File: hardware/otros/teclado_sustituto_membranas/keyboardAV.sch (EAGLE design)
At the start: 99 parts, among them IC1 74HC32, IC2 74LS244DW

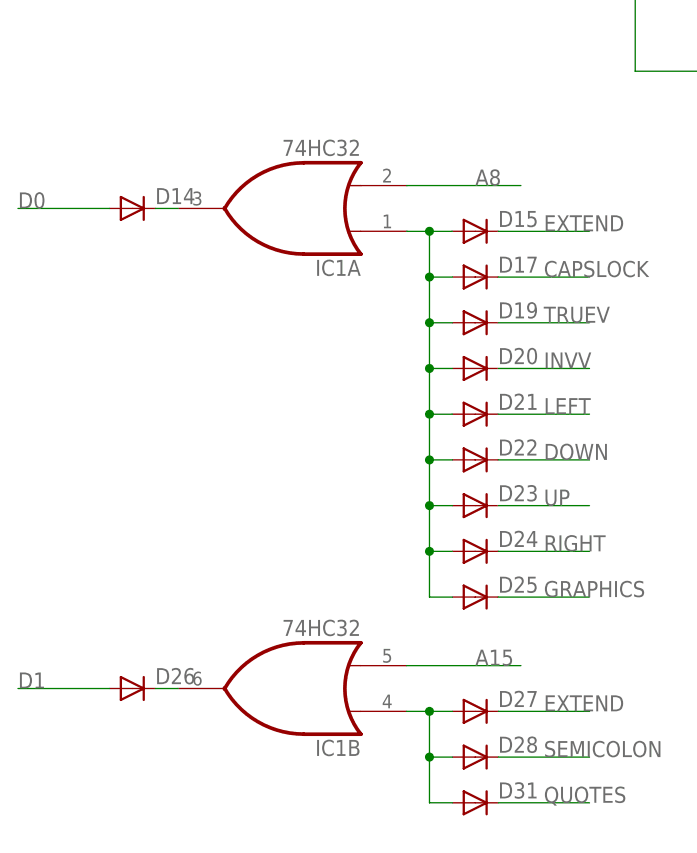
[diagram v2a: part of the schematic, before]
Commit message: 
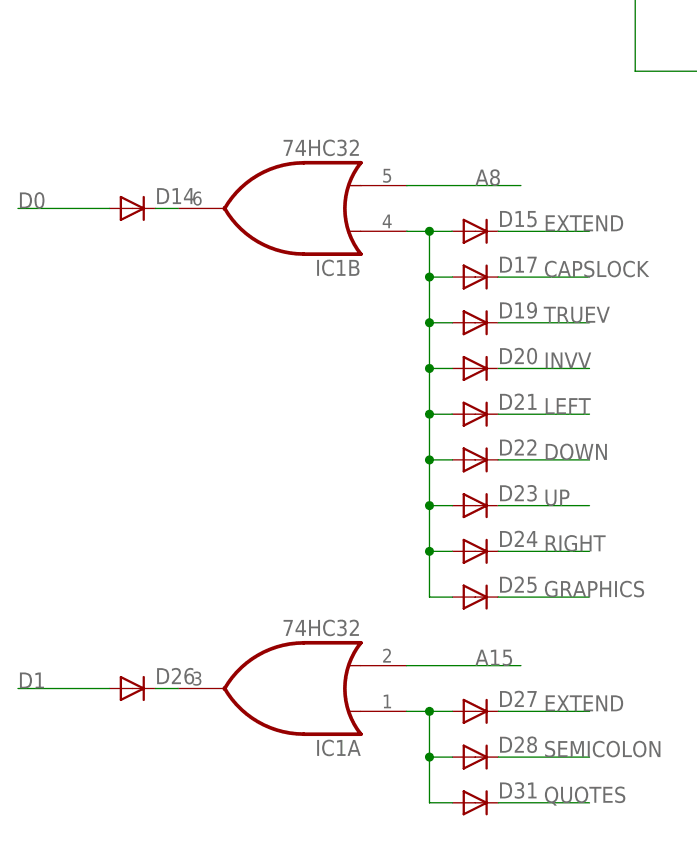
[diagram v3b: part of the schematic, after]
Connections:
- net A15: now also IC1A.I1; no longer IC1B.I1
- net A8: now also IC1B.I1; no longer IC1A.I1
- net N$84: now also IC1B.O; no longer IC1A.O
- net N$86: now also IC1A.O; no longer IC1B.O
- net N$87: now also IC1A.I0; no longer IC1B.I0
- net N$90: now also IC1B.I0; no longer IC1A.I0
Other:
- moved on the sheet: IC1A, IC1B
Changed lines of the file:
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@@
 <instance part="D29" gate="G$1" x="60.96" y="-55.88" rot="R180"/>
 <instance part="D30" gate="G$1" x="60.96" y="-58.42" rot="R180"/>
-<instance part="IC1" gate="A" x="-154.94" y="0" rot="R180"/>
-<instance part="IC1" gate="B" x="-154.94" y="-53.34" rot="R180"/>
+<instance part="IC1" gate="B" x="-154.94" y="0" rot="R180"/>
+<instance part="IC1" gate="A" x="-154.94" y="-53.34" rot="R180"/>
 <instance part="IC1" gate="C" x="129.54" y="-33.02" rot="R180"/>
 <instance part="IC1" gate="D" x="129.54" y="-50.8" rot="R180"/>
@@
 <wire x1="-142.24" y1="2.54" x2="-129.54" y2="2.54" width="0.1524" layer="91"/>
 <label x="-134.62" y="2.54" size="1.778" layer="95"/>
-<pinref part="IC1" gate="A" pin="I1"/>
+<pinref part="IC1" gate="B" pin="I1"/>
 </segment>
 </net>
@@
 <wire x1="-142.24" y1="-50.8" x2="-129.54" y2="-50.8" width="0.1524" layer="91"/>
 <label x="-134.62" y="-50.8" size="1.778" layer="95"/>
-<pinref part="IC1" gate="B" pin="I1"/>
+<pinref part="IC1" gate="A" pin="I1"/>
 </segment>
 <segment>
@@
 <wire x1="-137.16" y1="-7.62" x2="-139.7" y2="-7.62" width="0.1524" layer="91"/>
 <junction x="-139.7" y="-7.62"/>
-<pinref part="IC1" gate="A" pin="I0"/>
+<pinref part="IC1" gate="B" pin="I0"/>
 <pinref part="D15" gate="G$1" pin="A"/>
 <pinref part="D17" gate="G$1" pin="A"/>
@@
 <wire x1="-139.7" y1="-66.04" x2="-139.7" y2="-60.96" width="0.1524" layer="91"/>
 <junction x="-139.7" y="-60.96"/>
-<pinref part="IC1" gate="B" pin="I0"/>
+<pinref part="IC1" gate="A" pin="I0"/>
 <pinref part="D27" gate="G$1" pin="A"/>
 <pinref part="D28" gate="G$1" pin="A"/>
@@
 <net name="N$84" class="0">
 <segment>
-<pinref part="IC1" gate="A" pin="O"/>
+<pinref part="IC1" gate="B" pin="O"/>
 <wire x1="-167.64" y1="0" x2="-170.18" y2="0" width="0.1524" layer="91"/>
 <pinref part="D14" gate="G$1" pin="C"/>
@@
 <net name="N$86" class="0">
 <segment>
-<pinref part="IC1" gate="B" pin="O"/>
+<pinref part="IC1" gate="A" pin="O"/>
 <wire x1="-167.64" y1="-53.34" x2="-170.18" y2="-53.34" width="0.1524" layer="91"/>
 <pinref part="D26" gate="G$1" pin="C"/>
